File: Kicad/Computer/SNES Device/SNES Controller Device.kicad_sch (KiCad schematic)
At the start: 4 parts, among them J23 Conn_01x20_Male, J24 Conn_01x20_Female, J25 Conn_01x20_Female, J26 Conn_01x20_Male

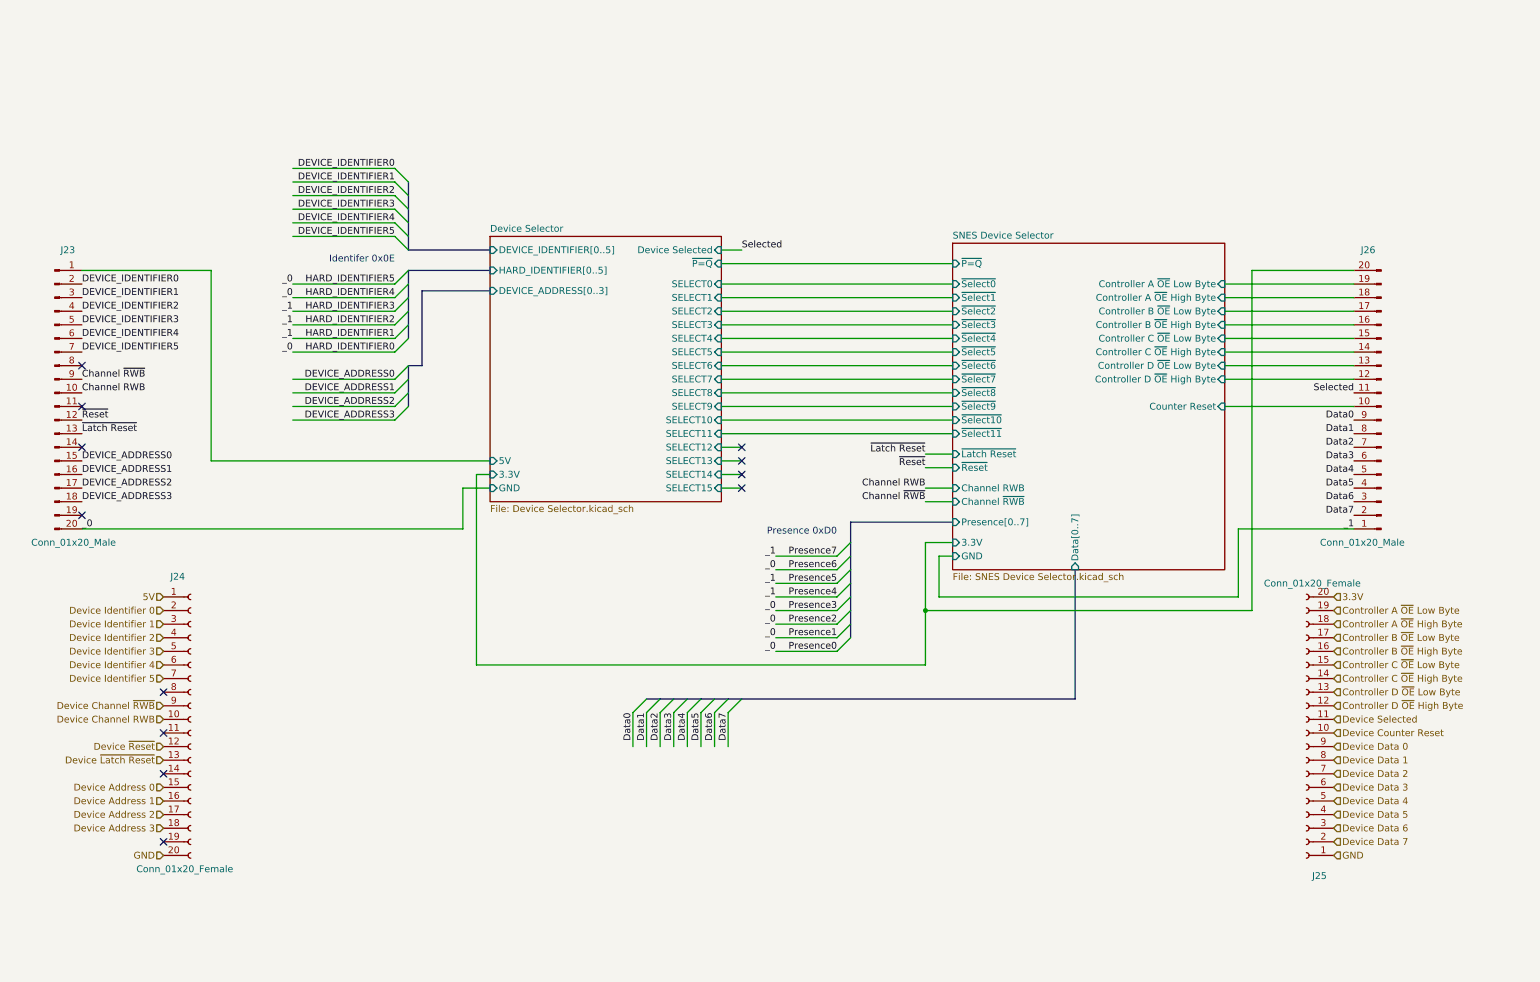
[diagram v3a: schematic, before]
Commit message: Split SNES device into multiple boards.
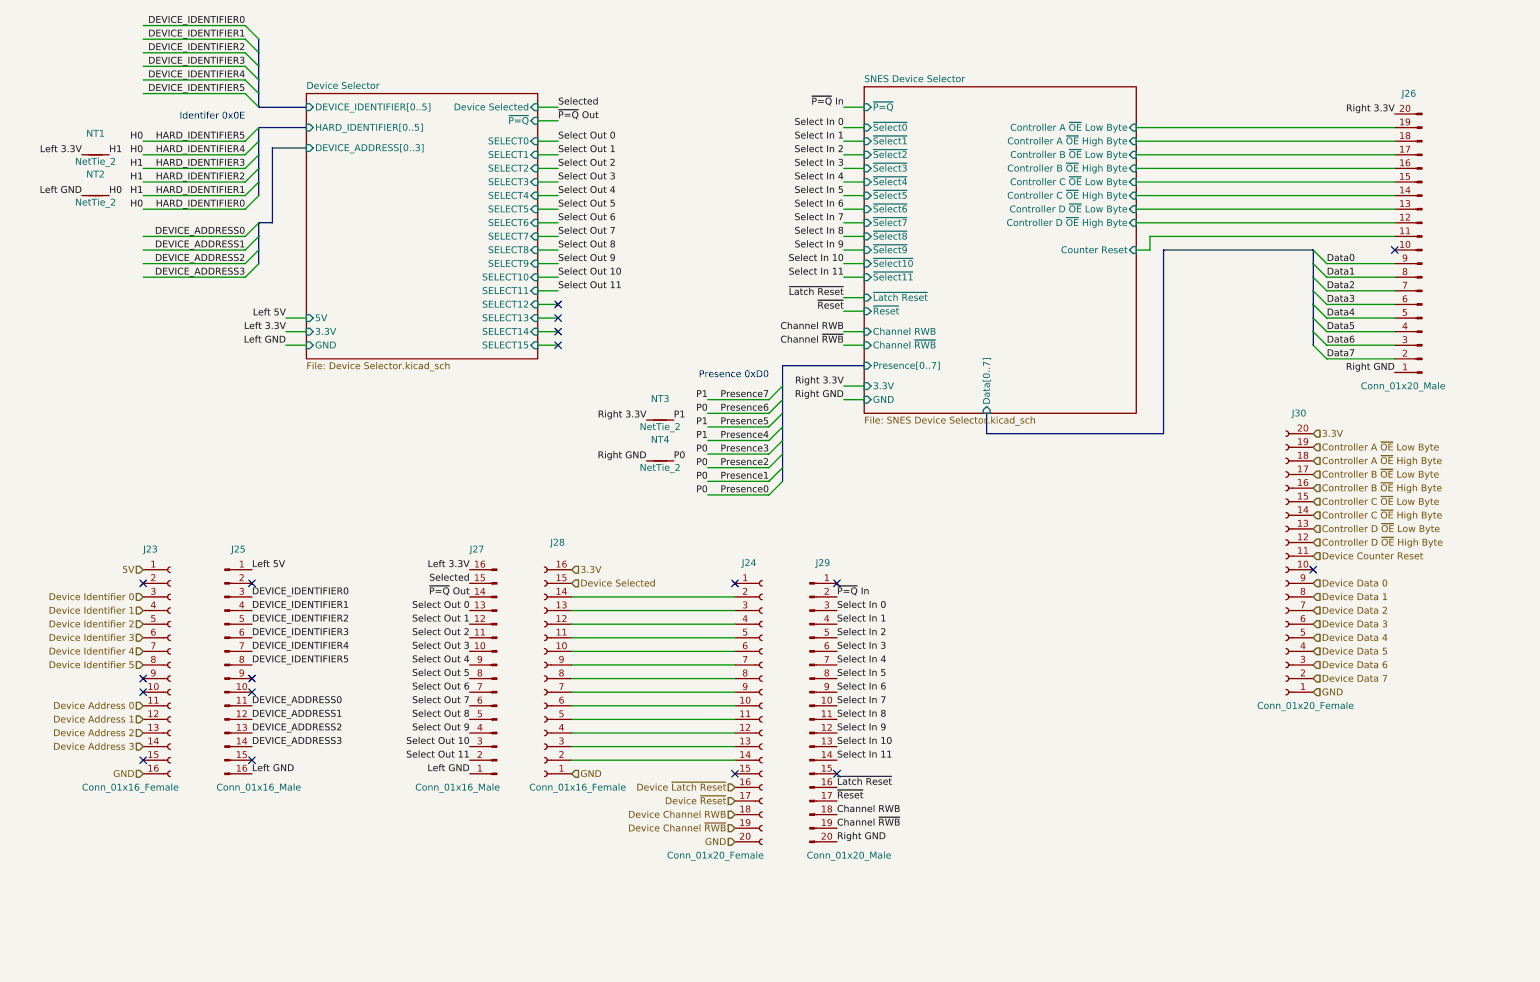
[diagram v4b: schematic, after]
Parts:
- removed J23: Conn_01x20_Male, Connector_PinHeader_2.54mm:PinHeader_1x20_P2.54mm_Vertical, symbol Connector:Conn_01x20_Male
- removed J25: Conn_01x20_Female, Connector_PinSocket_2.54mm:PinSocket_1x20_P2.54mm_Vertical, symbol Connector:Conn_01x20_Female
- added J23, J28: Conn_01x16_Female, Connector_PinSocket_2.54mm:PinSocket_1x16_P2.54mm_Vertical, symbol Connector:Conn_01x16_Female
- added J25, J27: Conn_01x16_Male, Connector_PinHeader_2.54mm:PinHeader_1x16_P2.54mm_Vertical, symbol Connector:Conn_01x16_Male
- added J29: Conn_01x20_Male, Connector_PinHeader_2.54mm:PinHeader_1x20_P2.54mm_Vertical, symbol Connector:Conn_01x20_Male
- added J30: Conn_01x20_Female, Connector_PinSocket_2.54mm:PinSocket_1x20_P2.54mm_Vertical, symbol Connector:Conn_01x20_Female
- added NT1, NT2, NT3, NT4: NetTie_2, NetTie:NetTie-2_SMD_Pad0.5mm, symbol Device:NetTie_2
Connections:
- net 3.3V: now also J28.16 (Pin_16), J30.20 (Pin_20)
- net 5V: now also J23.1 (Pin_1); no longer J24.1 (Pin_1)
- net Channel RWB: now also J29.18 (Pin_18)
- net Channel ~{RWB}: now also J29.19 (Pin_19)
- net Controller A ~{OE} High Byte: now also J30.18 (Pin_18)
- net Controller A ~{OE} Low Byte: now also J30.19 (Pin_19)
- net Controller B ~{OE} High Byte: now also J30.16 (Pin_16)
- net Controller B ~{OE} Low Byte: now also J30.17 (Pin_17)
- net Controller C ~{OE} High Byte: now also J30.14 (Pin_14)
- net Controller C ~{OE} Low Byte: now also J30.15 (Pin_15)
- net Controller D ~{OE} High Byte: now also J30.12 (Pin_12)
- net Controller D ~{OE} Low Byte: now also J30.13 (Pin_13)
- net DEVICE_ADDRESS0: now also J25.11 (Pin_11)
- net DEVICE_ADDRESS1: now also J25.12 (Pin_12)
- net DEVICE_ADDRESS2: now also J25.13 (Pin_13)
- net DEVICE_ADDRESS3: now also J25.14 (Pin_14)
- net DEVICE_IDENTIFIER0: now also J25.3 (Pin_3)
- net DEVICE_IDENTIFIER1: now also J25.4 (Pin_4)
- net DEVICE_IDENTIFIER2: now also J25.5 (Pin_5)
- net DEVICE_IDENTIFIER3: now also J25.6 (Pin_6)
- net DEVICE_IDENTIFIER4: now also J25.7 (Pin_7)
- net DEVICE_IDENTIFIER5: now also J25.8 (Pin_8)
- net Device Address 0: now also J23.11 (Pin_11); no longer J24.15 (Pin_15)
- net Device Address 1: now also J23.12 (Pin_12); no longer J24.16 (Pin_16)
- net Device Address 2: now also J23.13 (Pin_13); no longer J24.17 (Pin_17)
- net Device Address 3: now also J23.14 (Pin_14); no longer J24.18 (Pin_18)
- net Device Channel RWB: now also J24.18 (Pin_18); no longer J24.10 (Pin_10)
- net Device Channel ~{RWB}: now also J24.19 (Pin_19); no longer J24.9 (Pin_9)
- net Device Counter Reset: now also J30.11 (Pin_11)
- net Device Data 0: now also J30.9 (Pin_9)
- net Device Data 1: now also J30.8 (Pin_8)
- net Device Data 2: now also J30.7 (Pin_7)
- net Device Data 3: now also J30.6 (Pin_6)
- net Device Data 4: now also J30.5 (Pin_5)
- net Device Data 5: now also J30.4 (Pin_4)
- net Device Data 6: now also J30.3 (Pin_3)
- net Device Data 7: now also J30.2 (Pin_2)
- net Device Identifier 0: now also J23.3 (Pin_3); no longer J24.2 (Pin_2)
- net Device Identifier 1: now also J23.4 (Pin_4); no longer J24.3 (Pin_3)
- net Device Identifier 2: now also J23.5 (Pin_5); no longer J24.4 (Pin_4)
- net Device Identifier 3: now also J23.6 (Pin_6); no longer J24.5 (Pin_5)
- net Device Identifier 4: now also J23.7 (Pin_7); no longer J24.6 (Pin_6)
- net Device Identifier 5: now also J23.8 (Pin_8); no longer J24.7 (Pin_7)
- net Device Selected: now also J28.15 (Pin_15)
- net Device ~{Latch Reset}: now also J24.16 (Pin_16); no longer J24.13 (Pin_13)
- net Device ~{Reset}: now also J24.17 (Pin_17); no longer J24.12 (Pin_12)
- net GND: now also J23.16 (Pin_16), J28.1 (Pin_1), J30.1 (Pin_1)
- net SNES Device Selector/Counter Reset: now also J26.11 (Pin_11); no longer J26.10 (Pin_10)
- net Selected: now also J27.15 (Pin_15); no longer J26.11 (Pin_11)
- net ~{Latch Reset}: now also J29.16 (Pin_16)
- net ~{Reset}: now also J29.17 (Pin_17)
- net at J24.11 (Pin_11): now also J28.5 (Pin_5)
- net at J24.14 (Pin_14): now also J28.2 (Pin_2)
- net at J24.8 (Pin_8): now also J28.8 (Pin_8)
- net Device Selector/3.3V renamed Right 3.3V
- net Right 3.3V: now also NT3.1
- net HARD_IDENTIFIER1 renamed Right GND
- net Right GND: now also J29.20 (Pin_20), NT4.1
- new net: J24.10 (Pin_10), J28.6 (Pin_6)
- new net: J24.12 (Pin_12), J28.4 (Pin_4)
- new net: J24.13 (Pin_13), J28.3 (Pin_3)
- new net: J24.2 (Pin_2), J28.14 (Pin_14)
- new net: J24.3 (Pin_3), J28.13 (Pin_13)
- new net: J24.4 (Pin_4), J28.12 (Pin_12)
- new net: J24.5 (Pin_5), J28.11 (Pin_11)
- new net: J24.6 (Pin_6), J28.10 (Pin_10)
- new net: J24.7 (Pin_7), J28.9 (Pin_9)
- new net: J24.9 (Pin_9), J28.7 (Pin_7)
- new net H0: NT2.2
- new net H1: NT1.2
- new net Left 3.3V: J27.16 (Pin_16), NT1.1
- new net Left 5V: J25.1 (Pin_1)
- new net Left GND: J25.16 (Pin_16), J27.1 (Pin_1), NT2.1
- new net P0: NT4.2
- new net P1: NT3.2
- new net Select In 0: J29.3 (Pin_3)
- new net Select In 1: J29.4 (Pin_4)
- new net Select In 10: J29.13 (Pin_13)
- new net Select In 11: J29.14 (Pin_14)
- new net Select In 2: J29.5 (Pin_5)
- new net Select In 3: J29.6 (Pin_6)
- new net Select In 4: J29.7 (Pin_7)
- new net Select In 5: J29.8 (Pin_8)
- new net Select In 6: J29.9 (Pin_9)
- new net Select In 7: J29.10 (Pin_10)
- new net Select In 8: J29.11 (Pin_11)
- new net Select In 9: J29.12 (Pin_12)
- new net Select Out 0: J27.13 (Pin_13)
- new net Select Out 1: J27.12 (Pin_12)
- new net Select Out 10: J27.3 (Pin_3)
- new net Select Out 11: J27.2 (Pin_2)
- new net Select Out 2: J27.11 (Pin_11)
- new net Select Out 3: J27.10 (Pin_10)
- new net Select Out 4: J27.9 (Pin_9)
- new net Select Out 5: J27.8 (Pin_8)
- new net Select Out 6: J27.7 (Pin_7)
- new net Select Out 7: J27.6 (Pin_6)
- new net Select Out 8: J27.5 (Pin_5)
- new net Select Out 9: J27.4 (Pin_4)
- new net ~{P=Q} In: J29.2 (Pin_2)
- new net ~{P=Q} Out: J27.14 (Pin_14)
- no-connect marks 12 -> 18
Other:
- moved on the sheet: J24, J26
